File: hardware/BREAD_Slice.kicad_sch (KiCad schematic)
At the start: 15 parts, among them J1 Conn_01x10_Female, J2 I2C_01x04

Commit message: Initial commit
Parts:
- removed C1, C3, C4: 22uF, Capacitor_SMD:C_1206_3216Metric, symbol Device:C_Small
- removed C2: 100nF, Capacitor_SMD:C_1206_3216Metric, symbol Device:C_Small
- removed D1: WS2812B_5050, SparkFun-LED:WS2812-5050-4PIN, symbol SparkFun-LED:WS2812B_5050
- removed HS1: Heatsink_Pad, SparkFun-Fuse:Thermal Pad, symbol Mechanical:Heatsink_Pad
- removed J2: I2C_01x04, Connector_JST:JST_SH_SM04B-SRSS-TB_1x04-1MP_P1.00mm_Horizontal, symbol SparkFun-Connector:I2C_01x04
- removed L1: 4.7uH, Inductor_SMD:L_1210_3225Metric, symbol Device:L_Small
- removed U1: ~, Package_TO_SOT_SMD:TSOT-23-6, symbol SparkFun-DiscreteSemi:AP63205
- added C1, C2: 10uF_t, OCI_UPL_FOOTPRINTS:C_2312, symbol BREAD_Slice-rescue:10uF_t-OCI_UPL_2_Capacitors
- added C3: 100uF, OCI_UPL_FOOTPRINTS:C_Radial_D8_L11.5_P3.5, symbol Device:C
- added D1: D, OCI_UPL_FOOTPRINTS:Diode_DO-41_SOD81_Horizontal_RM10, symbol Device:D
- added J2, J3: Term_2, OCI_UPL_FOOTPRINTS:TerminalBlock_Pheonix_MKDS1.5-2pol, symbol BREAD_Slice-rescue:Term_2-OCI_UPL_10_Connectors
- added L1: 560 uH, Inductor_THT:L_Radial_D28.0mm_P29.20mm, symbol BREAD_Slice-rescue:INDUCTOR-pspice
- added Logo1: Logo_Open_Hardware_Small, Symbol:OSHW-Symbol_6.7x6mm_SilkScreen, symbol Graphic:Logo_Open_Hardware_Small
- added Q1: TIP120, OCI_UPL_FOOTPRINTS:TO-220_Neutral123_Vertical_LargePads, symbol BREAD_Slice-rescue:TIP120-OCI_UPL_4_Semiconductors
- added R1: 100k, Resistor_THT:R_Axial_DIN0309_L9.0mm_D3.2mm_P15.24mm_Horizontal, symbol Device:R_US
- added RV1: 100k, Potentiometer_THT:Potentiometer_Bourns_3266W_Vertical, symbol BREAD_Slice-rescue:R_POT_US-Device
- H1, H4: footprint MountingHole:MountingHole_5mm -> MountingHole:MountingHole_3.2mm_M3_DIN965_Pad
- H2: renamed from H3; footprint MountingHole:MountingHole_5mm -> MountingHole:MountingHole_3.2mm_M3_DIN965_Pad
- H3: renamed from H2; footprint MountingHole:MountingHole_5mm -> MountingHole:MountingHole_3.2mm_M3_DIN965_Pad
- J1: symbol Connector:Conn_01x10_Female -> BREAD_Slice-rescue:Conn_01x10_Female-Connector
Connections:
- net +12V: now also A1.30 (VIN), C1.1
- net +5V: now also C2.1
- net GND: now also C1.2, C2.2, C3.2, D1.2 (A), J2.1, J3.2, RV1.2, RV1.3
- net FB: now reaches A1.19 (A0)
- net FB: now also R1.2, RV1.1
- net SW: now reaches A1.9 (D6)
- net SW: now also Q1.1 (B)
- net LED: no longer names the net of A1.8 (D5)
- new net: J2.2, Q1.2 (C)
- new net: D1.1 (K), L1.1, Q1.3 (E)
- new net: C3.1, J3.1, L1.2, R1.1
- no-connect marks 22 -> 19
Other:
- moved on the sheet: A1, H1, H2, H3, H4, J1

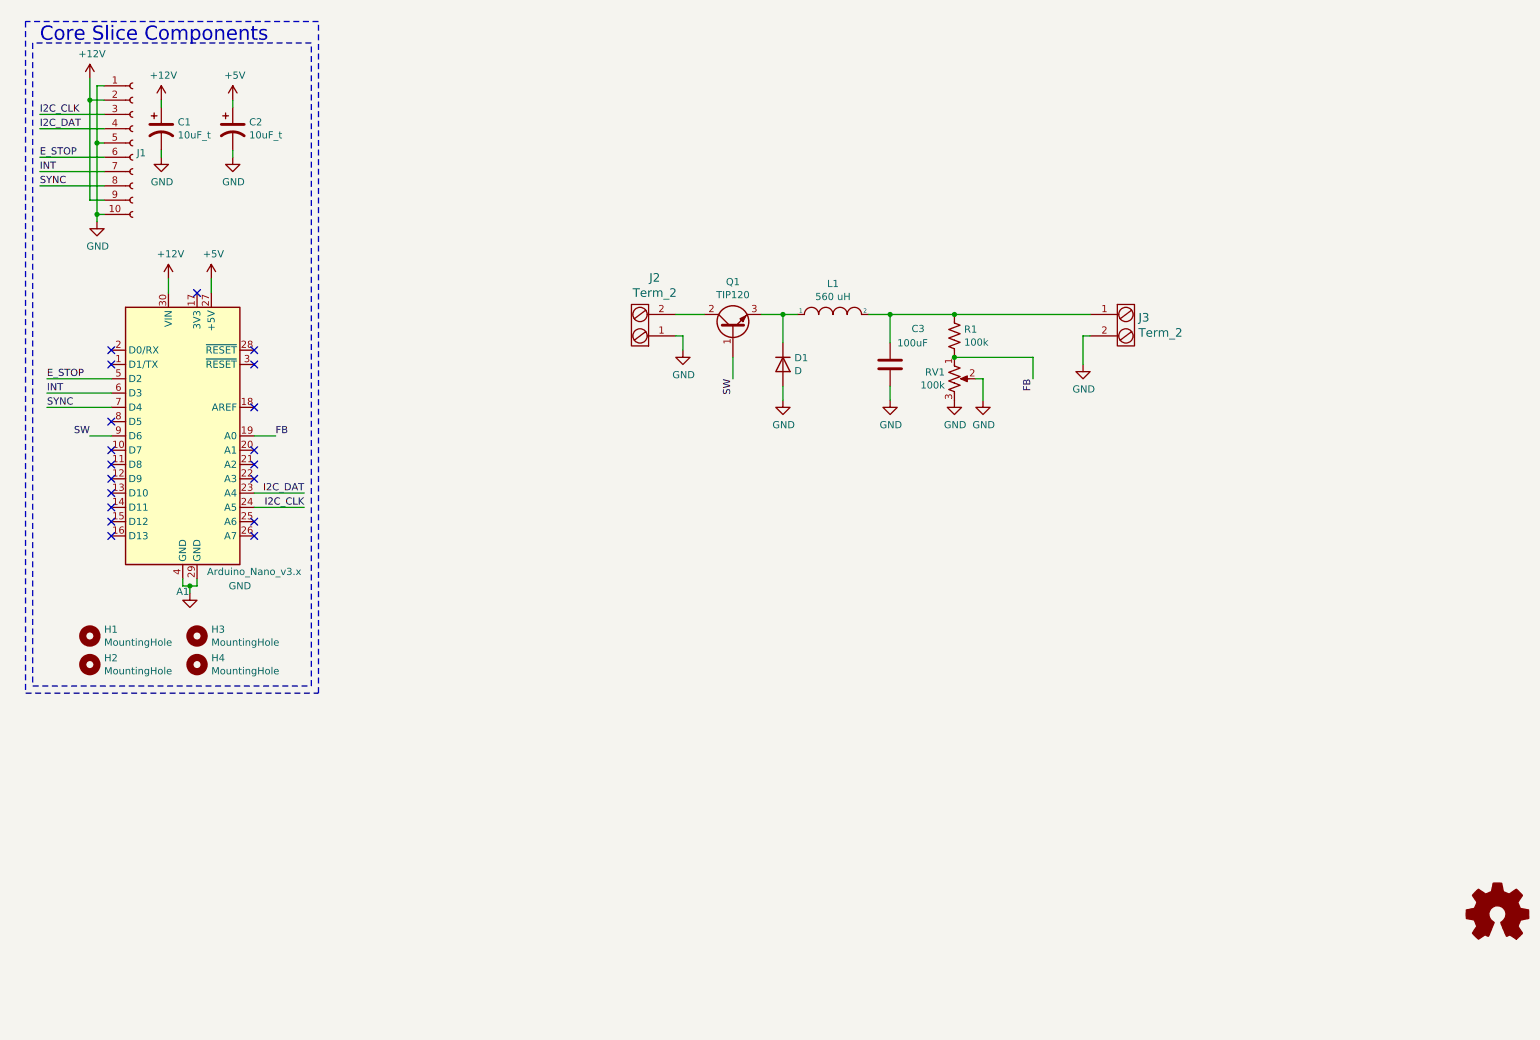
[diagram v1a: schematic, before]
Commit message: updated to new BREAD format
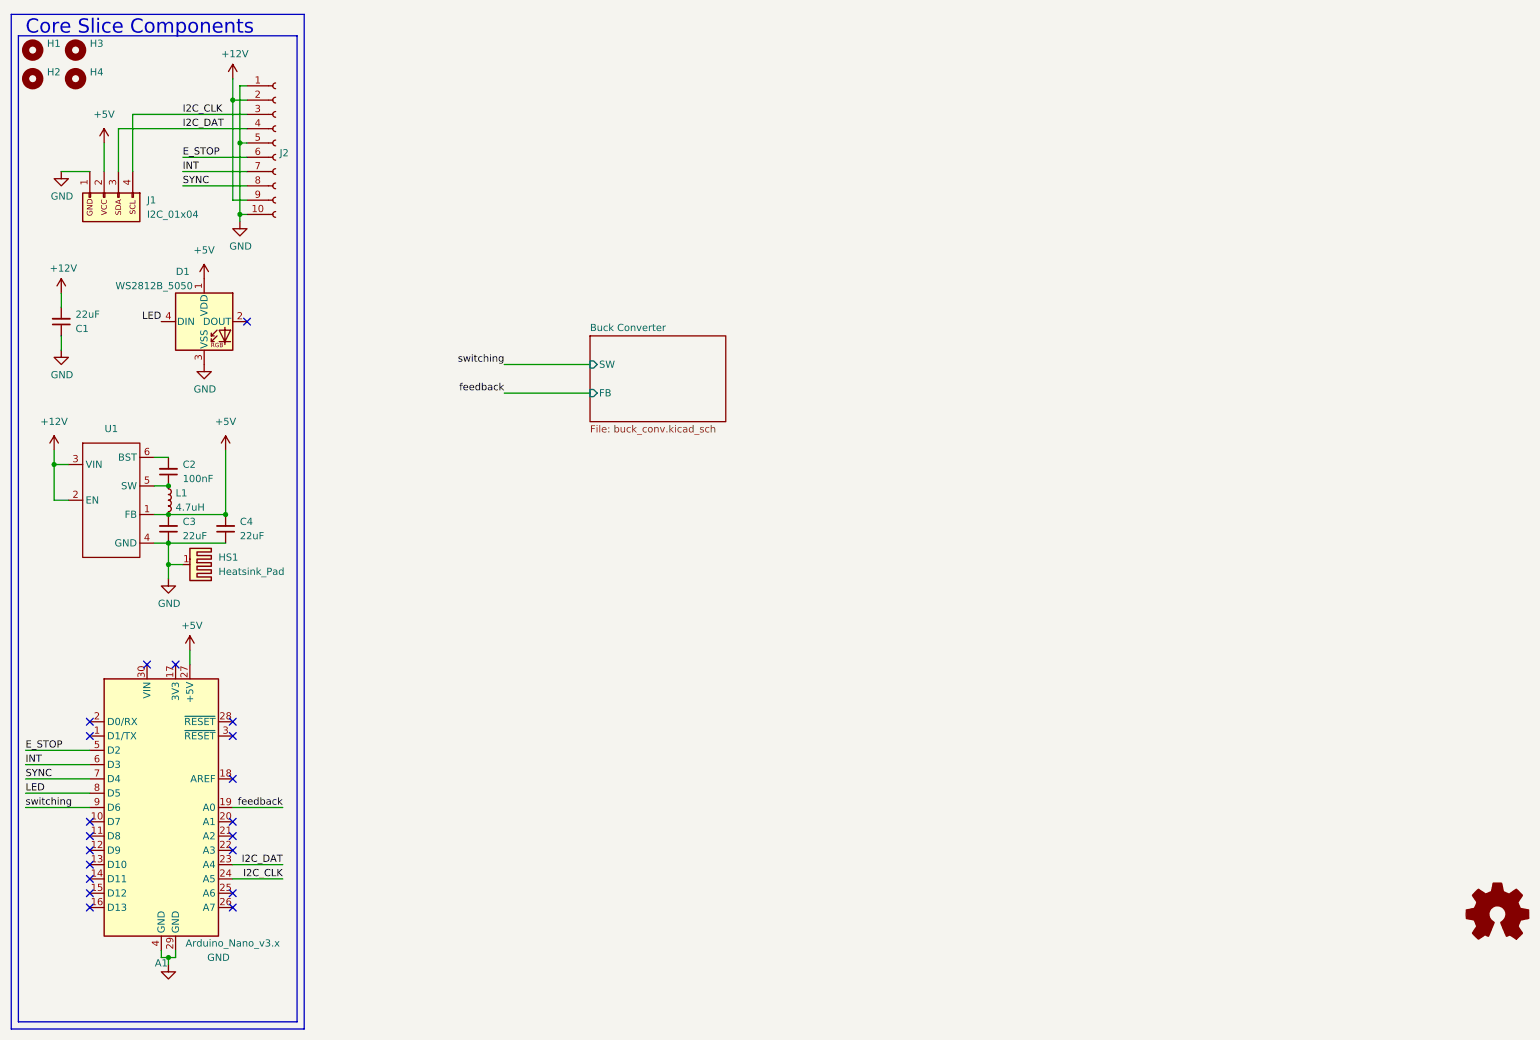
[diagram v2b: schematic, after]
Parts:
- removed C1, C2: 10uF_t, OCI_UPL_FOOTPRINTS:C_2312, symbol BREAD_Slice-rescue:10uF_t-OCI_UPL_2_Capacitors
- removed C3: 100uF, OCI_UPL_FOOTPRINTS:C_Radial_D8_L11.5_P3.5, symbol Device:C
- removed D1: D, OCI_UPL_FOOTPRINTS:Diode_DO-41_SOD81_Horizontal_RM10, symbol Device:D
- removed J2, J3: Term_2, OCI_UPL_FOOTPRINTS:TerminalBlock_Pheonix_MKDS1.5-2pol, symbol BREAD_Slice-rescue:Term_2-OCI_UPL_10_Connectors
- removed L1: 560 uH, Inductor_THT:L_Radial_D28.0mm_P29.20mm, symbol BREAD_Slice-rescue:INDUCTOR-pspice
- removed Logo1: Logo_Open_Hardware_Small, Symbol:OSHW-Symbol_6.7x6mm_SilkScreen, symbol Graphic:Logo_Open_Hardware_Small
- removed Q1: TIP120, OCI_UPL_FOOTPRINTS:TO-220_Neutral123_Vertical_LargePads, symbol BREAD_Slice-rescue:TIP120-OCI_UPL_4_Semiconductors
- removed R1: 100k, Resistor_THT:R_Axial_DIN0309_L9.0mm_D3.2mm_P15.24mm_Horizontal, symbol Device:R_US
- removed RV1: 100k, Potentiometer_THT:Potentiometer_Bourns_3266W_Vertical, symbol BREAD_Slice-rescue:R_POT_US-Device
- added C1, C3, C4: 22uF, Capacitor_SMD:C_1206_3216Metric, symbol Device:C_Small
- added C2: 100nF, Capacitor_SMD:C_1206_3216Metric, symbol Device:C_Small
- added D1: WS2812B_5050, SparkFun-LED:WS2812-5050-4PIN, symbol SparkFun-LED:WS2812B_5050
- added HS1: Heatsink_Pad, KML-Custom:Thermal Pad, symbol Mechanical:Heatsink_Pad
- added J1: I2C_01x04, Connector_JST:JST_SH_SM04B-SRSS-TB_1x04-1MP_P1.00mm_Horizontal, symbol SparkFun-Connector:I2C_01x04
- added L1: 4.7uH, Inductor_SMD:L_1210_3225Metric, symbol Device:L_Small
- added U1: ~, Package_TO_SOT_SMD:TSOT-23-6, symbol SparkFun-DiscreteSemi:AP63205
- H1, H4: footprint MountingHole:MountingHole_3.2mm_M3_DIN965_Pad -> MountingHole:MountingHole_5mm
- H2: renamed from H3; footprint MountingHole:MountingHole_3.2mm_M3_DIN965_Pad -> MountingHole:MountingHole_5mm
- H3: renamed from H2; footprint MountingHole:MountingHole_3.2mm_M3_DIN965_Pad -> MountingHole:MountingHole_5mm
- J2: renamed from J1; symbol BREAD_Slice-rescue:Conn_01x10_Female-Connector -> Connector:Conn_01x10_Female
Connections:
- net +12V: now also C1.2, U1.2 (EN), U1.3 (VIN); no longer A1.30 (VIN)
- net +5V: now also C3.2, C4.2, D1.1 (VDD), J1.2 (Pin_2), L1.2, U1.1 (FB)
- net GND: now also C1.1, C3.1, C4.1, D1.3 (VSS), HS1.1, J1.1 (Pin_1), U1.4 (GND)
- net I2C_CLK: now also J1.4 (Pin_4)
- net I2C_DAT: now also J1.3 (Pin_3)
- net LED: now reaches A1.8 (D5)
- net LED: now also D1.4 (DIN)
- net FB renamed feedback
- net SW renamed switching
- new net: C2.1, L1.1, U1.5 (SW)
- new net: C2.2, U1.6 (BST)
- no-connect marks 19 -> 20
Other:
- added sheet Buck Converter (buck_conv.kicad_sch)
- moved on the sheet: A1, H1, H2, H3, H4, J2

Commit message: JLCPCB order rev-A
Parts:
- added J3, J4, J5, J6: Term_PressFit_1x01_5mm_Phoenix_Contact_1751066, KML-Custom:1751066, symbol kml-custom:Term_PressFit_1x01_5mm_Phoenix_Contact_1751066
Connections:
- net GND: now also J4.1, J4.2, J6.1, J6.2
- new net Buck Converter/in: J3.1, J3.2
- new net Buck Converter/out: J5.1, J5.2
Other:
- sheet Buck Converter ports: added GND, in, out; removed none
